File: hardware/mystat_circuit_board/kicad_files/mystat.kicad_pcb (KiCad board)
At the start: 4 copper layers, 60 x 81 mm, 93 parts, among them J1 PJ-063AH, J2 2173157-3, J3 SJ1-42534-SMT, K1 9011-05-11, K2 9011-05-11, K3 9011-05-11, K4 9011-05-11, K5 9011-05-11, P1 ICSP, U10 OPA192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

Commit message: Add files via upload
new version from KiCad 6.0
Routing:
- net GND: track 635.0 -> 633.1 mm
- net +13.4V: track 159.4 -> 158.4 mm
- net Net-(J2-Pad3): track 54.0 -> 53.0 mm
- net I_MEAS: track 57.2 -> 56.6 mm
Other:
- net class Default removed

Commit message: Add files via upload
Minor re-routing tracks on PCB to pass KiCad 7.0 design rules checks
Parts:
- U9: value DAC1220 -> SSOP-16_3.9x4.9mm_P0.635mm
- moved C37 0.80 mm to (76.5, 65.4)
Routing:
- net GND: track 633.1 -> 638.9 mm
- net -13.4V: track 178.8 -> 176.3 mm
- net RANGE2: track 38.7 -> 40.8 mm
- net I_MEAS: track 56.6 -> 55.6 mm
- net RANGE3: track 37.4 -> 38.2 mm

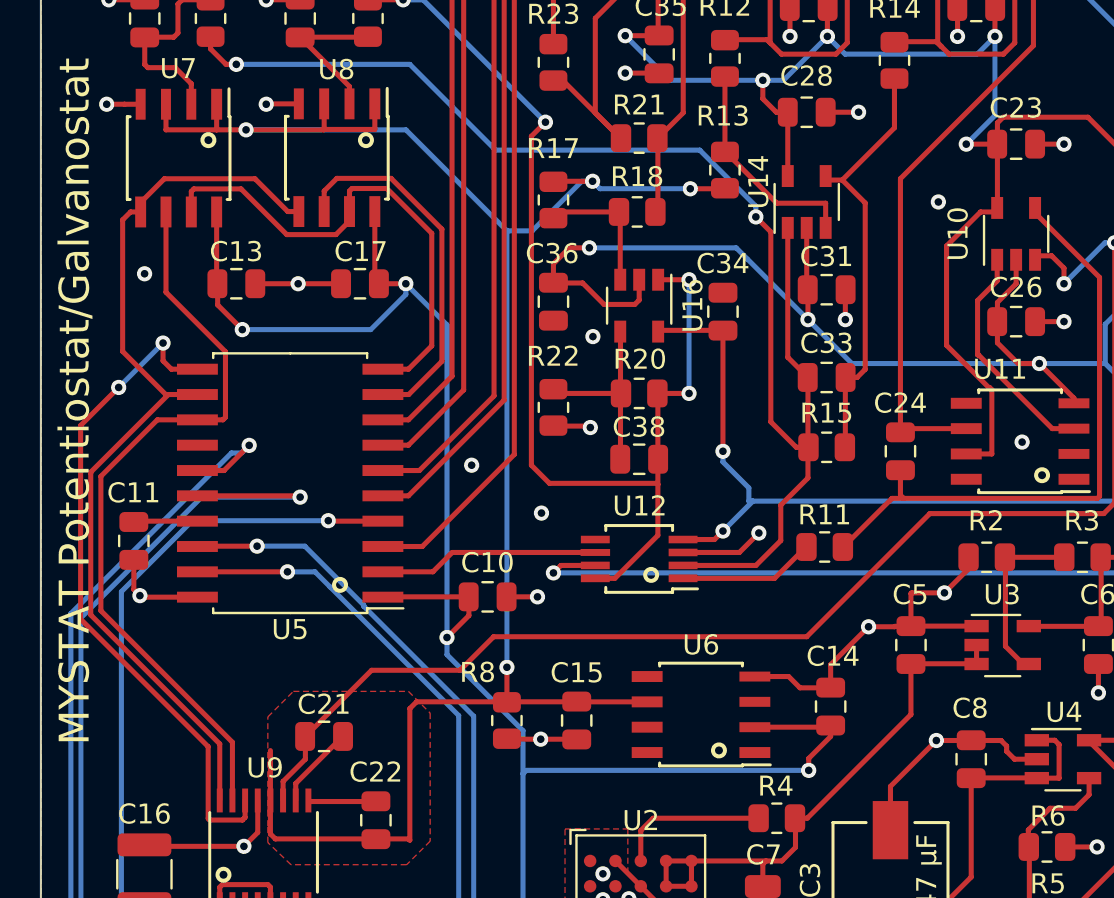
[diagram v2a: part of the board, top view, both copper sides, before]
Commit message: Add files via upload
Minor routing change and edit back silkscreen.
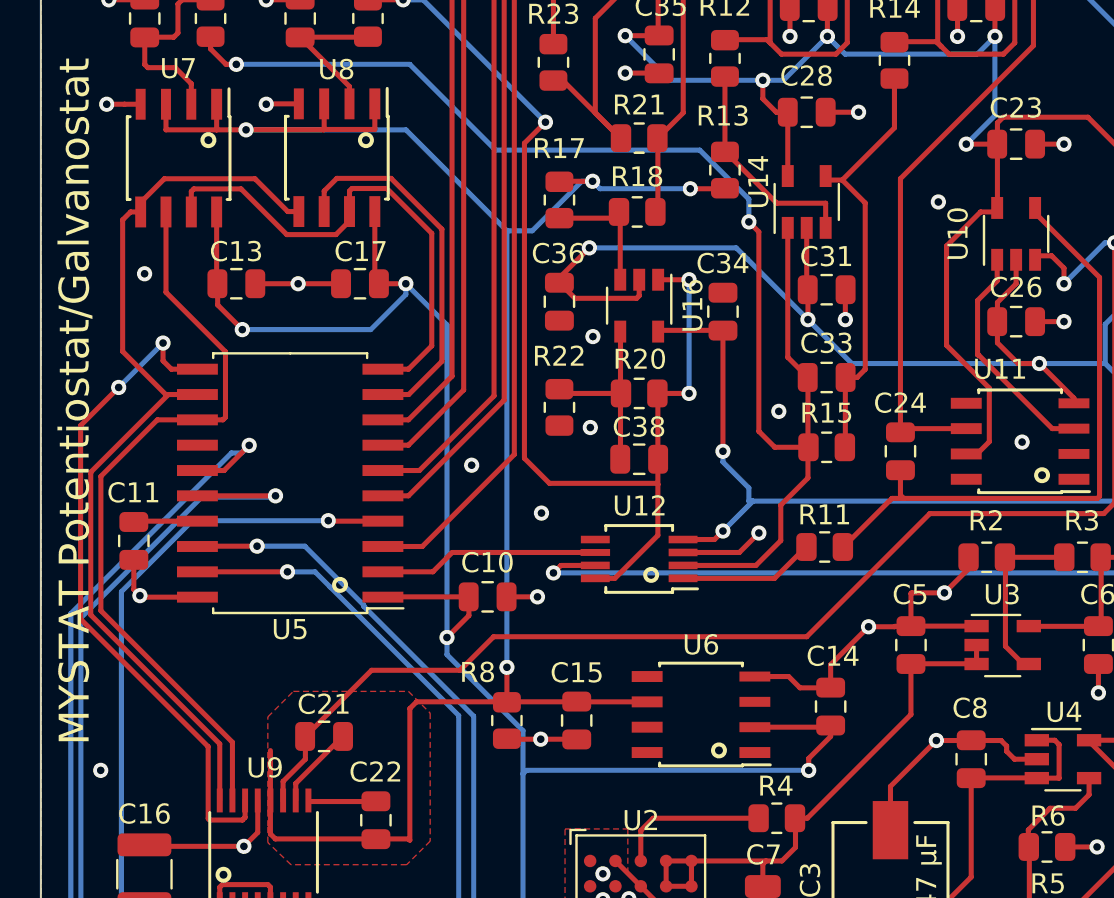
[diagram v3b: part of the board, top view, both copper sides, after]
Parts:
- moved C36 0.30 mm to (76.0, 83.0)
- moved R17 0.30 mm to (76.0, 77.9)
- moved R22 0.30 mm to (76.0, 88.3)
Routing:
- net Net-(P1-Pad4): track 50.8 -> 48.3 mm
- net GND: track 638.9 -> 637.1 mm, vias 55 -> 57
- net -13.4V: track 176.3 -> 175.2 mm
- net V_MEAS: track 67.0 -> 67.6 mm
- net +13.4V: track 158.4 -> 157.8 mm
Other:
- board text added: "Version 8 is great!"
- board text removed: "Lucky version 7"
